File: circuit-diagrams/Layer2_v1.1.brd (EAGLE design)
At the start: 40.6 x 40.6 mm, 9 parts

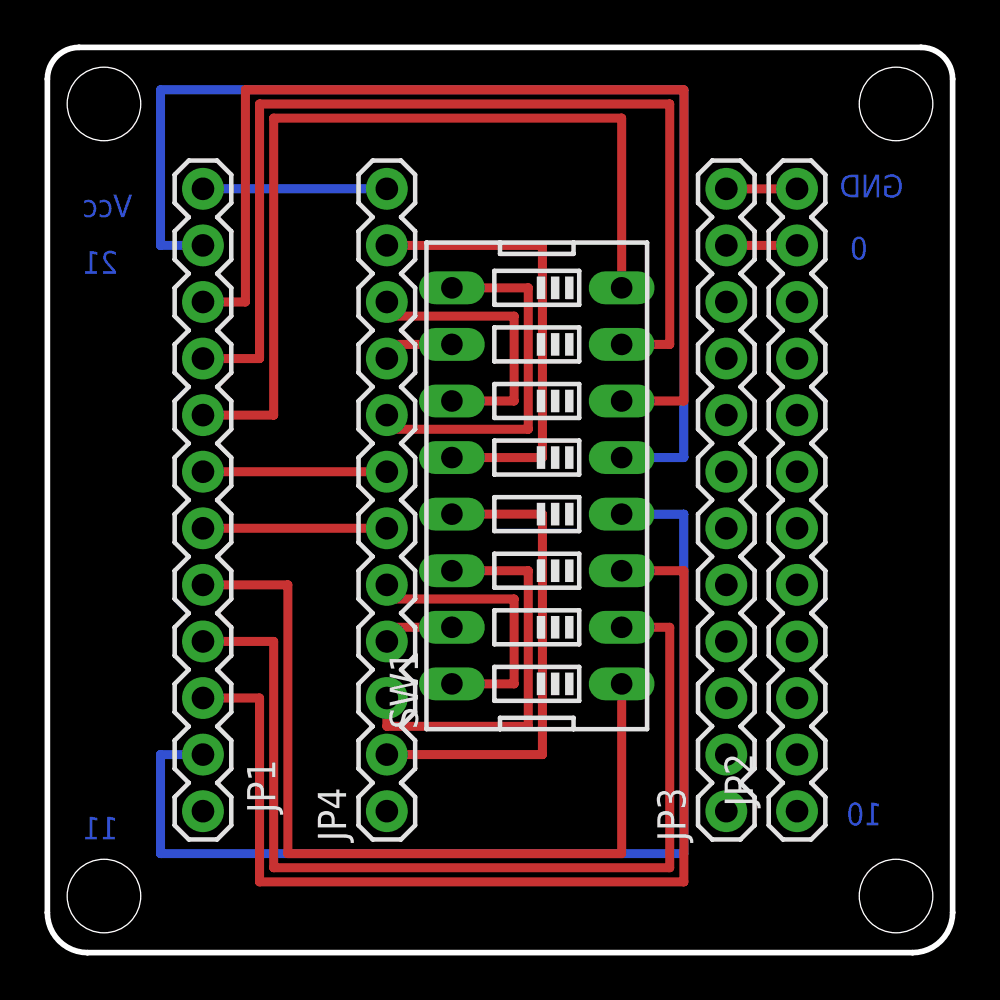
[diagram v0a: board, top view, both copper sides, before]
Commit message: Fixed mapping of pins in layer 2 in v1.1
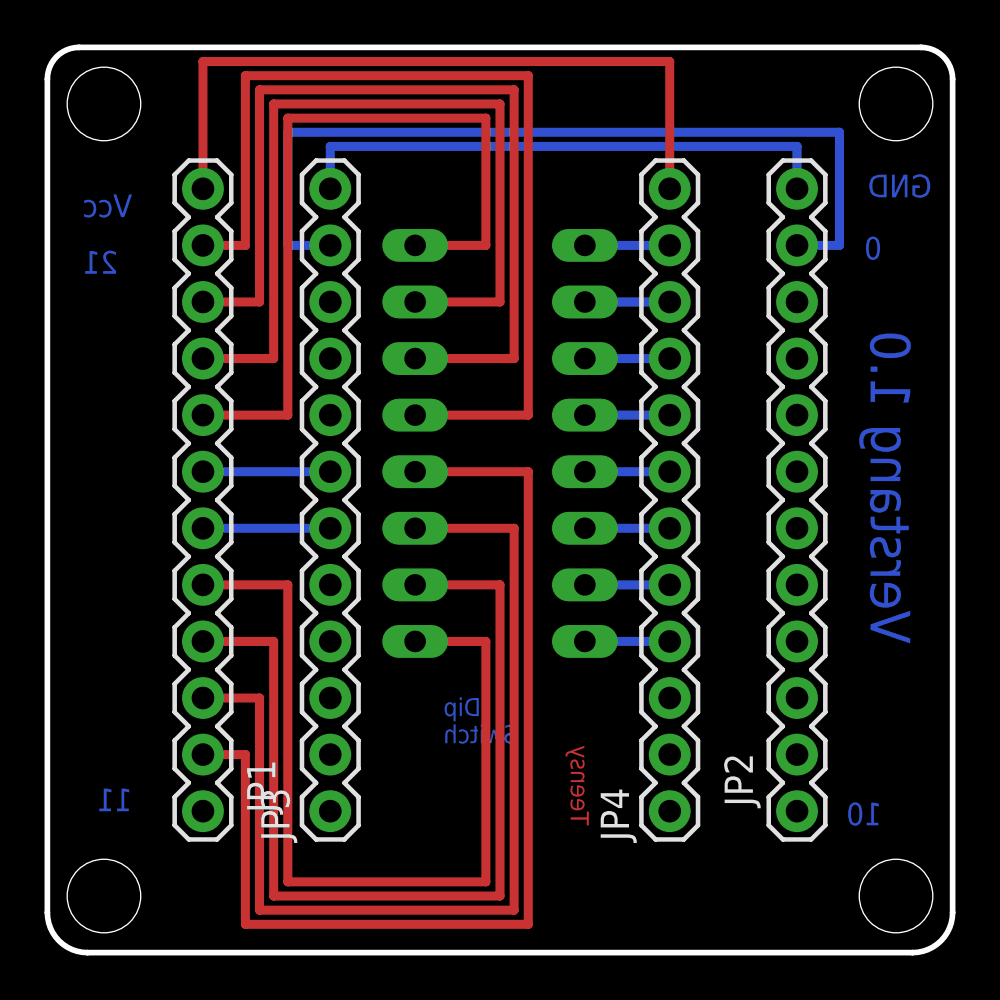
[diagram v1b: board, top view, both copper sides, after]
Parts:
- moved JP3 17.8 mm to (12.7, 6.35)
- moved JP4 12.7 mm to (27.9, 6.35)
- moved SW1 2.52 mm to (20.3, 22.9), flipped to the bottom
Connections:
- removed net T12B3: JP4.2, SW1.13
- removed net T13B2: JP4.3, SW1.14
- removed net T14B1: JP4.4, SW1.15
- removed net T15B0: JP4.5, SW1.16
- removed net T18B7: JP4.8, SW1.9
- removed net T19B6: JP4.9, SW1.10
- removed net T20B5: JP4.10, SW1.11
- removed net T21B4: JP4.11, SW1.12
- new net T14B0: JP4.4, SW1.16
- new net T15B1: JP4.5, SW1.15
- new net T16B2: JP4.6, SW1.14
- new net T17B3: JP4.7, SW1.13
- new net T18B4: JP4.8, SW1.12
- new net T19B5: JP4.9, SW1.11
- new net T20B6: JP4.10, SW1.10
- new net T21B7: JP4.11, SW1.9
- net P16B8: now also JP3.6; no longer JP4.6
- net P17B9: now also JP3.7; no longer JP4.7
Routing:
- net P0LWH: track 3.18 -> 38.7 mm
- net VCC: track 8.25 -> 32.4 mm
- net T12B3: track 21.8 -> 0.00 mm
- net GND: track 3.18 -> 24.8 mm
- net T21B4: track 20.6 -> 0.00 mm
- net T13B2: track 18.0 -> 0.00 mm
- net T18B7: track 16.8 -> 0.00 mm
- net T15B0: track 13.0 -> 0.00 mm
- net T20B5: track 13.0 -> 0.00 mm
- net P21B4: track 51.7 -> 42.5 mm
- net P20B5: track 47.9 -> 40.0 mm
- net P19B6: track 45.3 -> 37.5 mm
- net P18B7: track 39.8 -> 34.9 mm
- net T21B7: track 0.00 -> 3.81 mm
- net T20B6: track 0.00 -> 3.81 mm
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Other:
- board text added: "Dip Switch"
- board text added: "Teensy"
- board text added: "Verstang 1.0"
